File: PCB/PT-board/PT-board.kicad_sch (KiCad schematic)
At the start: 15 parts, among them J1 Screw_Terminal_01x02, J2 Screw_Terminal_01x02, J3 Conn_01x03_Female, J4 Conn_01x03_Male, U1 MAX31865ATP+

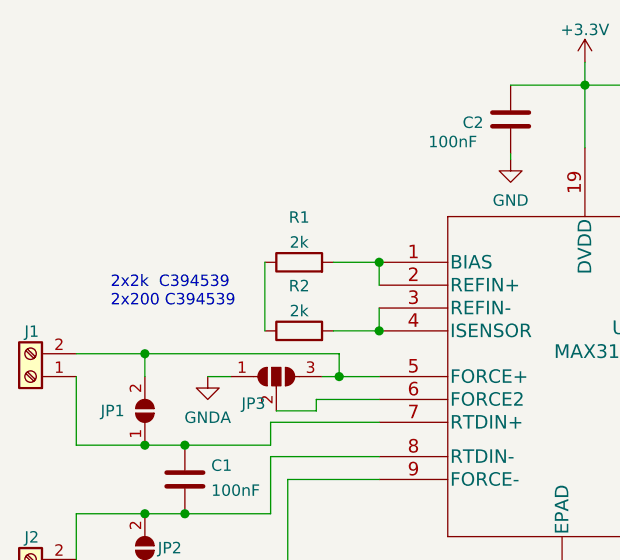
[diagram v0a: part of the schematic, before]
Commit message: Added K-type thermocouple board based on MAX31855.
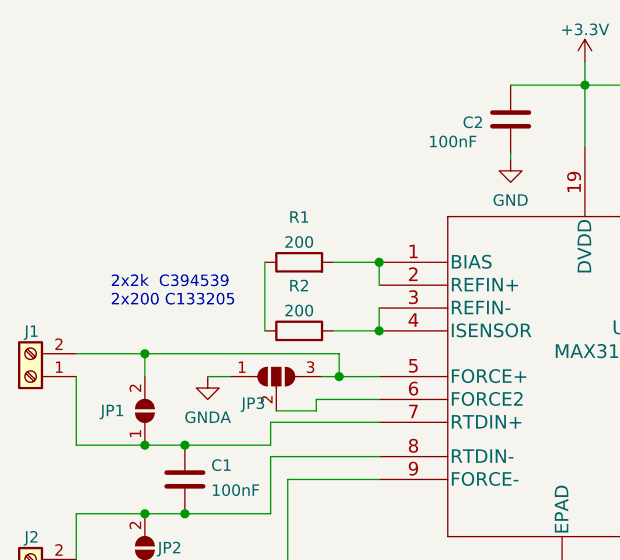
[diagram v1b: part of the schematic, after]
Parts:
- R1, R2: value 2k -> 200; LCSC C394539 -> C133205
- U1: LCSC (none) -> C404011
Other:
- note added: "2x2k C394539 2x200 C133205"
- note removed: "2x2k C394539 2x200 C394539"
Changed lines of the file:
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@@
     (stroke (width 0) (type solid) (color 0 0 0 0))
   )
-  (text "2x2k  C394539\n2x200 C394539" (at 73.66 67.31 0)
+  (text "2x2k  C394539\n2x200 C133205" (at 73.66 67.31 0)
     (effects (font (size 1.27 1.27)) (justify left bottom))
   )
@@
     (in_bom yes) (on_board yes) (fields_autoplaced)
     (property "Reference" "R1" (id 0) (at 94.615 57.2474 90))
-    (property "Value" "2k" (id 1) (at 94.615 60.0225 90))
+    (property "Value" "200" (id 1) (at 94.615 60.0225 90))
     (property "Footprint" "Resistor_SMD:R_0603_1608Metric" (id 2) (at 94.615 64.008 90)
       (effects (font (size 1.27 1.27)) hide)
@@
       (effects (font (size 1.27 1.27)) hide)
     )
-    (property "LCSC" "C394539" (id 4) (at 94.615 62.23 90)
+    (property "LCSC" "C133205" (id 4) (at 94.615 62.23 90)
       (effects (font (size 1.27 1.27)) hide)
     )
@@
     (in_bom yes) (on_board yes) (fields_autoplaced)
     (property "Reference" "R2" (id 0) (at 94.615 64.8674 90))
-    (property "Value" "2k" (id 1) (at 94.615 67.6425 90))
+    (property "Value" "200" (id 1) (at 94.615 67.6425 90))
     (property "Footprint" "Resistor_SMD:R_0603_1608Metric" (id 2) (at 94.615 71.628 90)
       (effects (font (size 1.27 1.27)) hide)
@@
       (effects (font (size 1.27 1.27)) hide)
     )
-    (property "LCSC" "C394539" (id 4) (at 94.615 69.85 90)
+    (property "LCSC" "C133205" (id 4) (at 94.615 69.85 90)
       (effects (font (size 1.27 1.27)) hide)
     )
@@
     (property "Datasheet" "" (id 3) (at 103.505 62.23 0)
       (effects (font (size 1.524 1.524)))
+    )
+    (property "LCSC" "C404011" (id 4) (at 103.505 62.23 0)
+      (effects (font (size 1.27 1.27)) hide)
     )
     (pin "1")
@@
     )
     (path "/adc13c6c-2812-43c7-95d0-730fad0184b2"
-      (reference "R1") (unit 1) (value "2k") (footprint "Resistor_SMD:R_0603_1608Metric")
+      (reference "R1") (unit 1) (value "200") (footprint "Resistor_SMD:R_0603_1608Metric")
     )
     (path "/eeabac59-68c9-4218-9b91-51be79bdebab"
-      (reference "R2") (unit 1) (value "2k") (footprint "Resistor_SMD:R_0603_1608Metric")
+      (reference "R2") (unit 1) (value "200") (footprint "Resistor_SMD:R_0603_1608Metric")
     )
     (path "/cdffe002-736d-4954-946b-e8813b1101b5"
